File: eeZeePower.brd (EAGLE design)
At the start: 25.9 x 12.7 mm, 11 parts

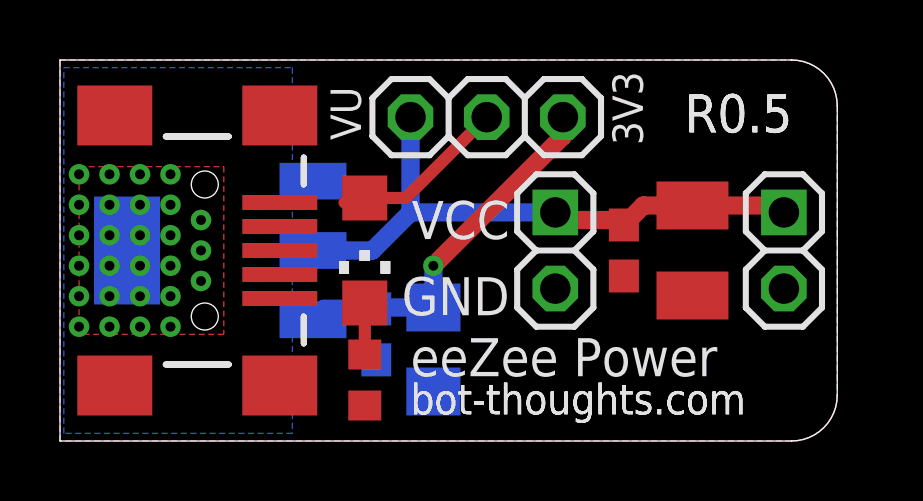
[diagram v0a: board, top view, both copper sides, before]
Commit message: Switched to TC1262 regulator, improved thermal design, moved jumper and LED around.
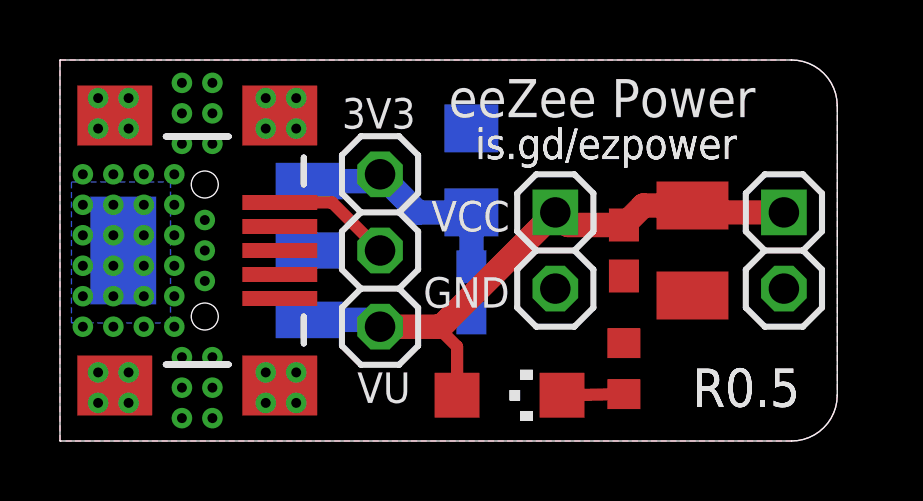
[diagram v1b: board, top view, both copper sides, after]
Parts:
- removed U1: (no value), SparkFun:SOT223
- added U2: TC1262_VDB, bt_regulator:SOT-223-3
- moved R1 8.64 mm to (18.8, 2.41), turned to 270 degrees
- moved LED1 6.82 mm to (15.0, 1.52), turned to 270 degrees
- moved C1 6.10 mm to (13.7, 9.02), turned to 90 degrees
- moved JP10 5.69 mm to (10.7, 6.35), turned to 270 degrees
- moved C2 3.47 mm to (13.7, 4.95)
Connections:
- net GND: now also U2.2, U2.4; no longer U1.1
- net VBUS: no longer LED1.A
- net VIN: now also U2.1; no longer U1.3
- net VOUT: now also LED1.A, U2.3; no longer U1.2, U1.4
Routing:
- net VIN: track 12.3 -> 7.85 mm, vias 1 -> 0
- net VBUS: track 5.87 -> 4.00 mm
- net VOUT: track 20.0 -> 20.6 mm, vias 27 -> 0
- removed copper zone on layer 1, net VOUT
- removed copper zone on layer 16, net VOUT
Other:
- board text added: "is.gd/ezpower"
- board text removed: "bot-thoughts.com"
